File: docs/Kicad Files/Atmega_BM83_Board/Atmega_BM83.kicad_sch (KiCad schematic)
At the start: 34 parts, among them J1 18V, J10 ICE Header, J2 Out to Amp, J3 PWR SW, J4 Volume POT, J5 Pairing BTN, J6 PWR LED, J7 Pair LED, J8 Conn_01x12, J9 Conn_01x12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

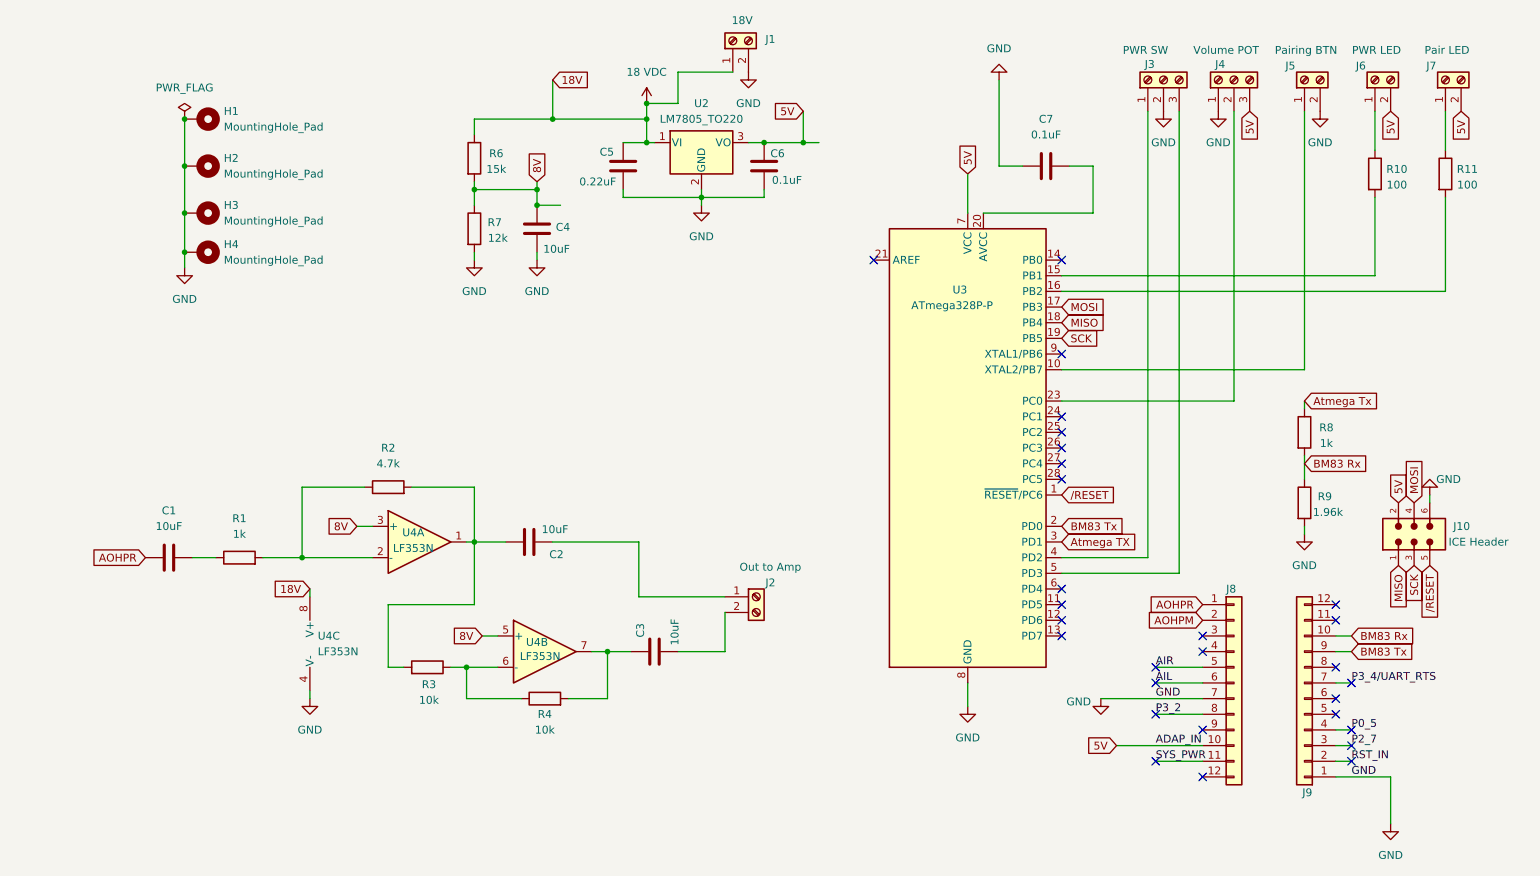
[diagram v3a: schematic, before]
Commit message: initial trace routing for MC/BM83 PCB complete
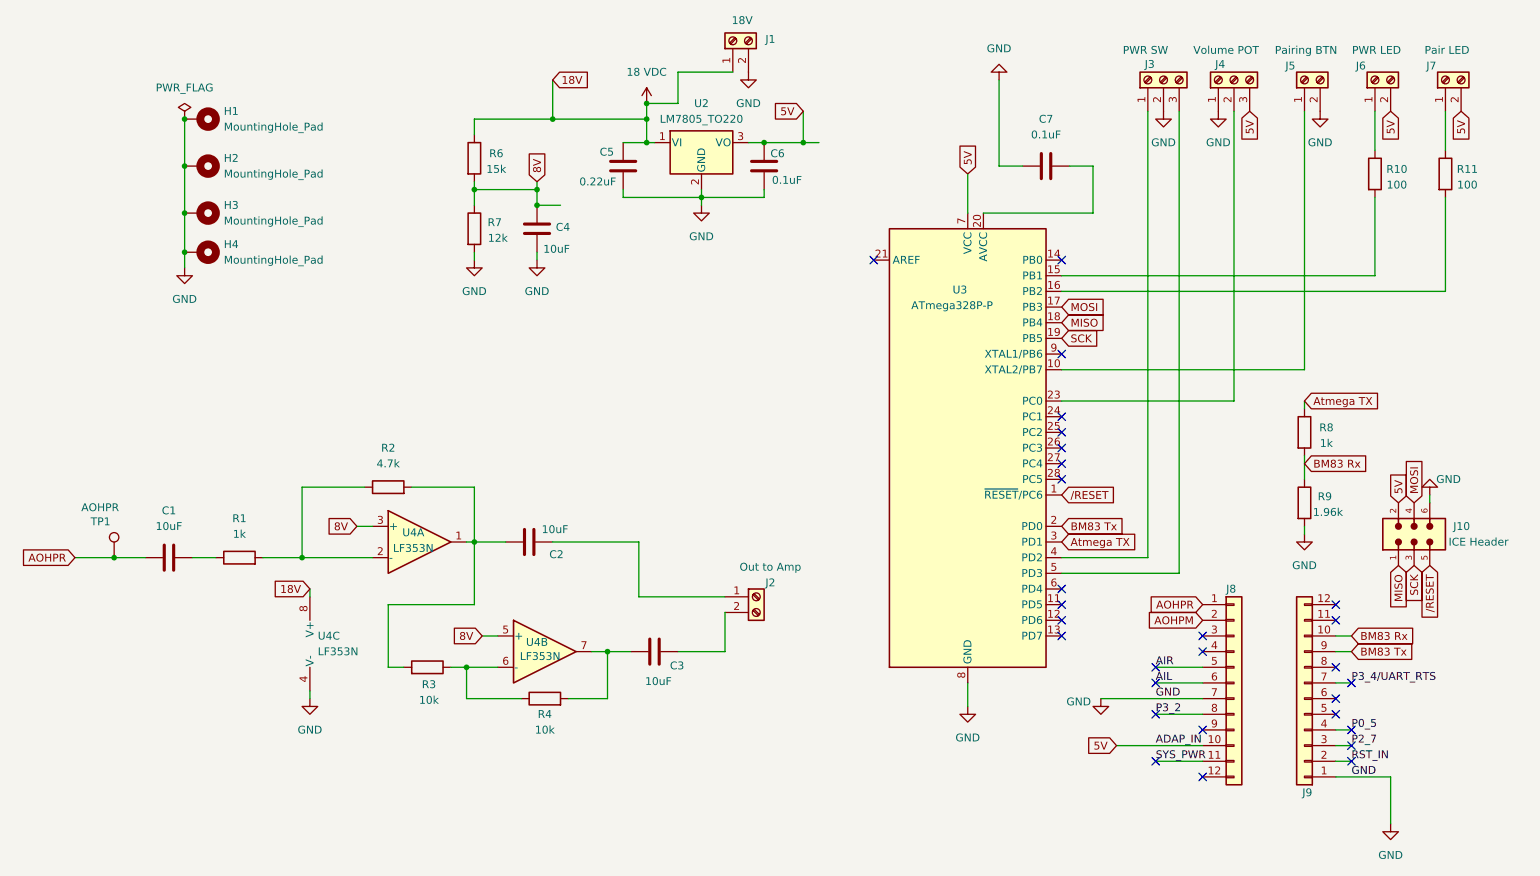
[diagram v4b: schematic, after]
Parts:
- added TP1: AOHPR, TestPoint:TestPoint_THTPad_D2.0mm_Drill1.0mm, symbol Connector:TestPoint
- J10: footprint Custom_Footprints:ICE_Header -> Z_Custom_Footprints:ICE_Header
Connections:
- net Atmega Tx is gone; now on net Atmega TX: R8.1
- net AOHPR: now also TP1.1
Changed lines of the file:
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@@
 	)
 	(junction
+		(at 57.15 102.87)
+		(diameter 0)
+		(color 0 0 0 0)
+	)
+	(junction
 		(at 162.56 35.56)
 		(diameter 0)
@@
 	(wire
 		(pts
+			(xy 57.15 102.87) (xy 62.23 102.87)
+		)
+		(stroke
+			(width 0)
+			(type default)
+		)
+	)
+	(wire
+		(pts
 			(xy 255.27 138.43) (xy 264.16 138.43)
 		)
@@
 	(wire
 		(pts
+			(xy 50.8 102.87) (xy 57.15 102.87)
+		)
+		(stroke
+			(width 0)
+			(type default)
+		)
+	)
+	(wire
+		(pts
 			(xy 101.6 110.49) (xy 115.57 110.49)
 		)
@@
 	(global_label "AOHPR"
 		(shape input)
-		(at 62.23 102.87 180)
+		(at 50.8 102.87 180)
 		(fields_autoplaced yes)
 		(effects
@@
 		)
 		(property "Intersheetrefs" "${INTERSHEET_REFS}"
-			(at 52.9552 102.87 0)
+			(at 41.5252 102.87 0)
 			(effects
 				(font
@@
 		)
 	)
-	(global_label "AOHPR"
+	(global_label "Atmega TX"
 		(shape input)
-		(at 233.68 110.49 180)
+		(at 250.19 77.47 0)
 		(fields_autoplaced yes)
 		(effects
@@
 				(size 1.27 1.27)
 			)
-			(justify right)
+			(justify left)
 		)
 		(property "Intersheetrefs" "${INTERSHEET_REFS}"
-			(at 224.4052 110.49 0)
+			(at 263.2141 77.47 0)
 			(effects
 				(font
 					(size 1.27 1.27)
 				)
-				(justify right)
+				(justify left)
 				(hide yes)
 			)
 		)
 	)
-	(global_label "Atmega Tx"
+	(global_label "AOHPR"
 		(shape input)
-		(at 250.19 77.47 0)
+		(at 233.68 110.49 180)
 		(fields_autoplaced yes)
 		(effects
@@
 				(size 1.27 1.27)
 			)
-			(justify left)
+			(justify right)
 		)
 		(property "Intersheetrefs" "${INTERSHEET_REFS}"
-			(at 263.0327 77.47 0)
+			(at 224.4052 110.49 0)
 			(effects
 				(font
 					(size 1.27 1.27)
 				)
-				(justify left)
+				(justify right)
 				(hide yes)
 			)
@@
 		(dnp no)
 		(property "Reference" "C3"
-			(at 142.494 115.824 0)
+			(at 149.606 120.396 90)
 			(effects
 				(font
@@
 		)
 		(property "Value" "10uF"
-			(at 148.082 117.094 0)
+			(at 147.574 122.936 90)
 			(effects
 				(font
@@
 			)
 		)
-		(property "Footprint" "Custom_Footprints:ICE_Header"
+		(property "Footprint" "Z_Custom_Footprints:ICE_Header"
 			(at 267.97 99.06 0)
 			(effects
@@
 					(unit 1)
 				)
+			)
+		)
+	)
+	(symbol
+		(lib_id "Connector:TestPoint")
+		(at 57.15 102.87 0)
+		(unit 1)
+		(exclude_from_sim no)
+		(in_bom yes)
+		(on_board yes)
+		(dnp no)
+		(property "Reference" "TP1"
+			(at 53.34 97.028 0)
+			(effects
+				(font
+					(size 1.27 1.27)
+				)
+				(justify left)
+			)
+		)
+		(property "Value" "AOHPR"
+			(at 51.816 94.742 0)
+			(effects
+				(font
+					(size 1.27 1.27)
+				)
+				(justify left)
+			)
+		)
+		(property "Footprint" "TestPoint:TestPoint_THTPad_D2.0mm_Drill1.0mm"
+			(at 62.23 102.87 0)
+			(effects
+				(font
+					(size 1.27 1.27)
+				)
+				(hide yes)
+			)
+		)
+		(property "Datasheet" "~"
+			(at 62.23 102.87 0)
+			(effects
+				(font
+					(size 1.27 1.27)
+				)
+				(hide yes)
+			)
+		)
+		(property "Description" "test point"
+			(at 57.15 102.87 0)
+			(effects
+				(font
+					(size 1.27 1.27)
+				)
+				(hide yes)
+			)
+		)
+		(pin "1"
+		)
+		(instances
+			(project ""
+				(path "/b3cfe92d-97c3-48fc-9671-6e68a58d7c48"
+					(reference "TP1")
+					(unit 1)
+				)

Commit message: final changes to both PCBs before review
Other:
- title: BM83/MC Module -> BT/MC Module
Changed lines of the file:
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@@
 	(paper "A4")
 	(title_block
-		(title "BM83/MC Module")
+		(title "BT/MC Module")
+		(date "2024-10-13")
+		(rev "A")
 	)
 	(junction

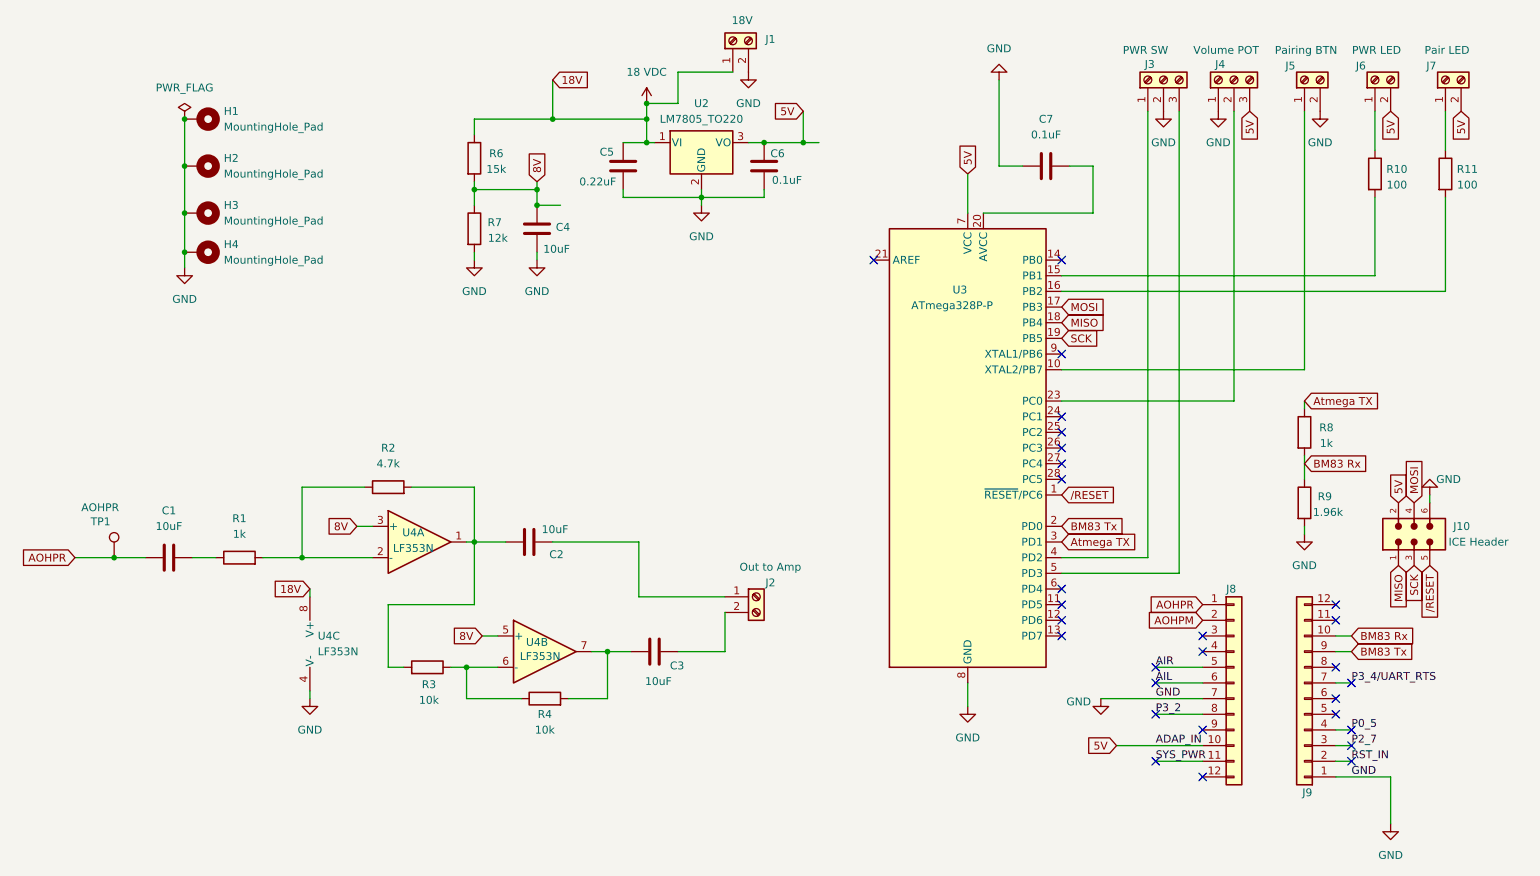
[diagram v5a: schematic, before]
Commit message: widened traces per Mark's suggestion. connected  AVCC and C7 as per datasheet.
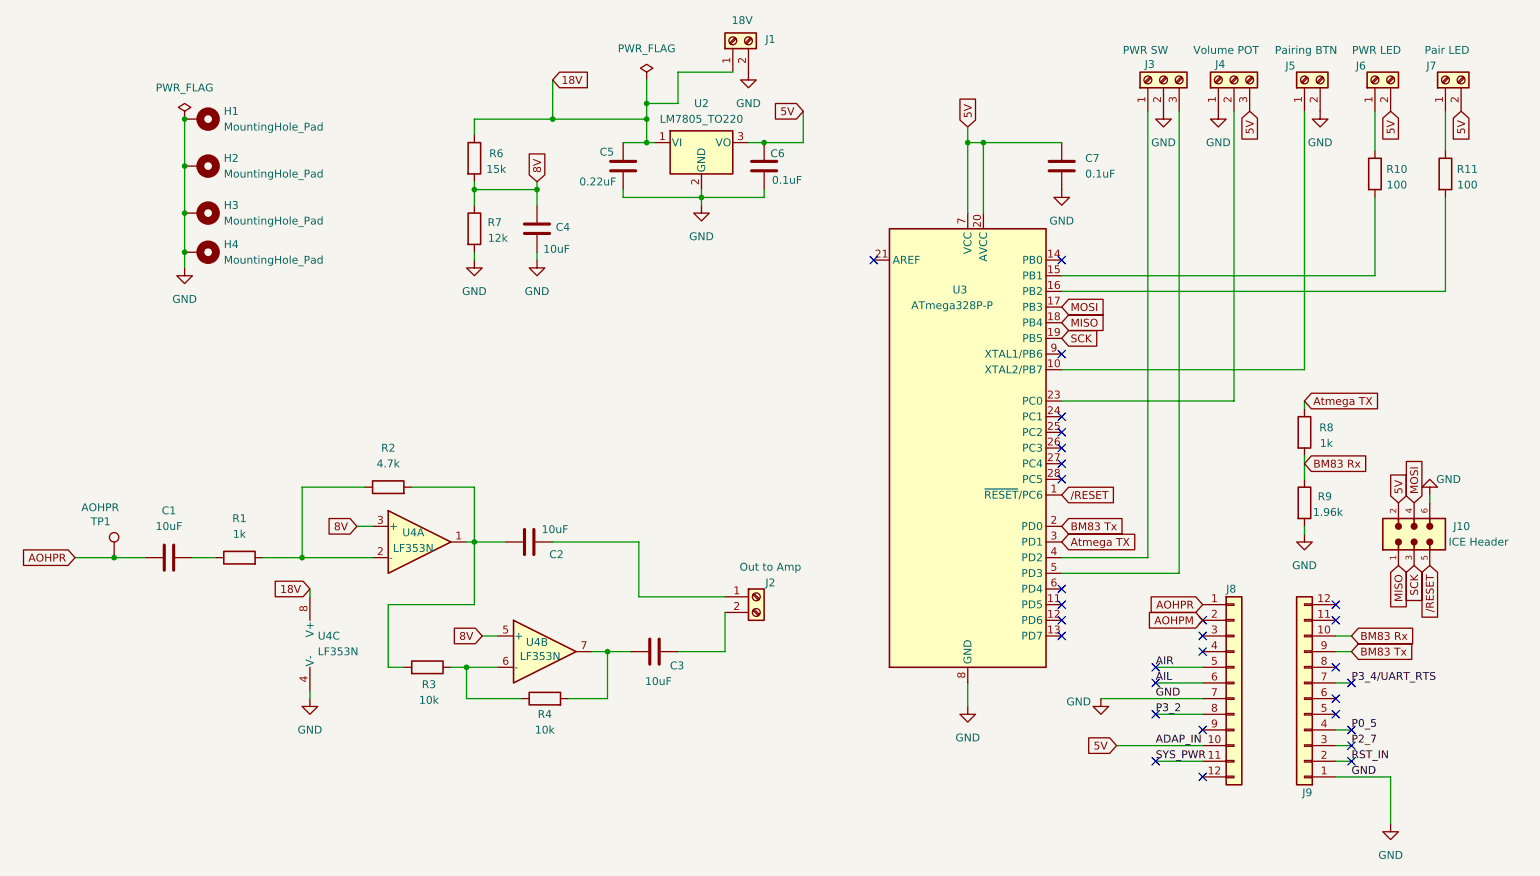
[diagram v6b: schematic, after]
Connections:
- net 5V: now also C7.1, U3.20 (AVCC)
- net GND: now also C7.2; no longer C7.1
- net 18 VDC renamed 18V
- no-connect marks 29 -> 30
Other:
- moved on the sheet: C7

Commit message: updated BT/MC board to reflect changes: removed C2 and C3, changed some cap locations
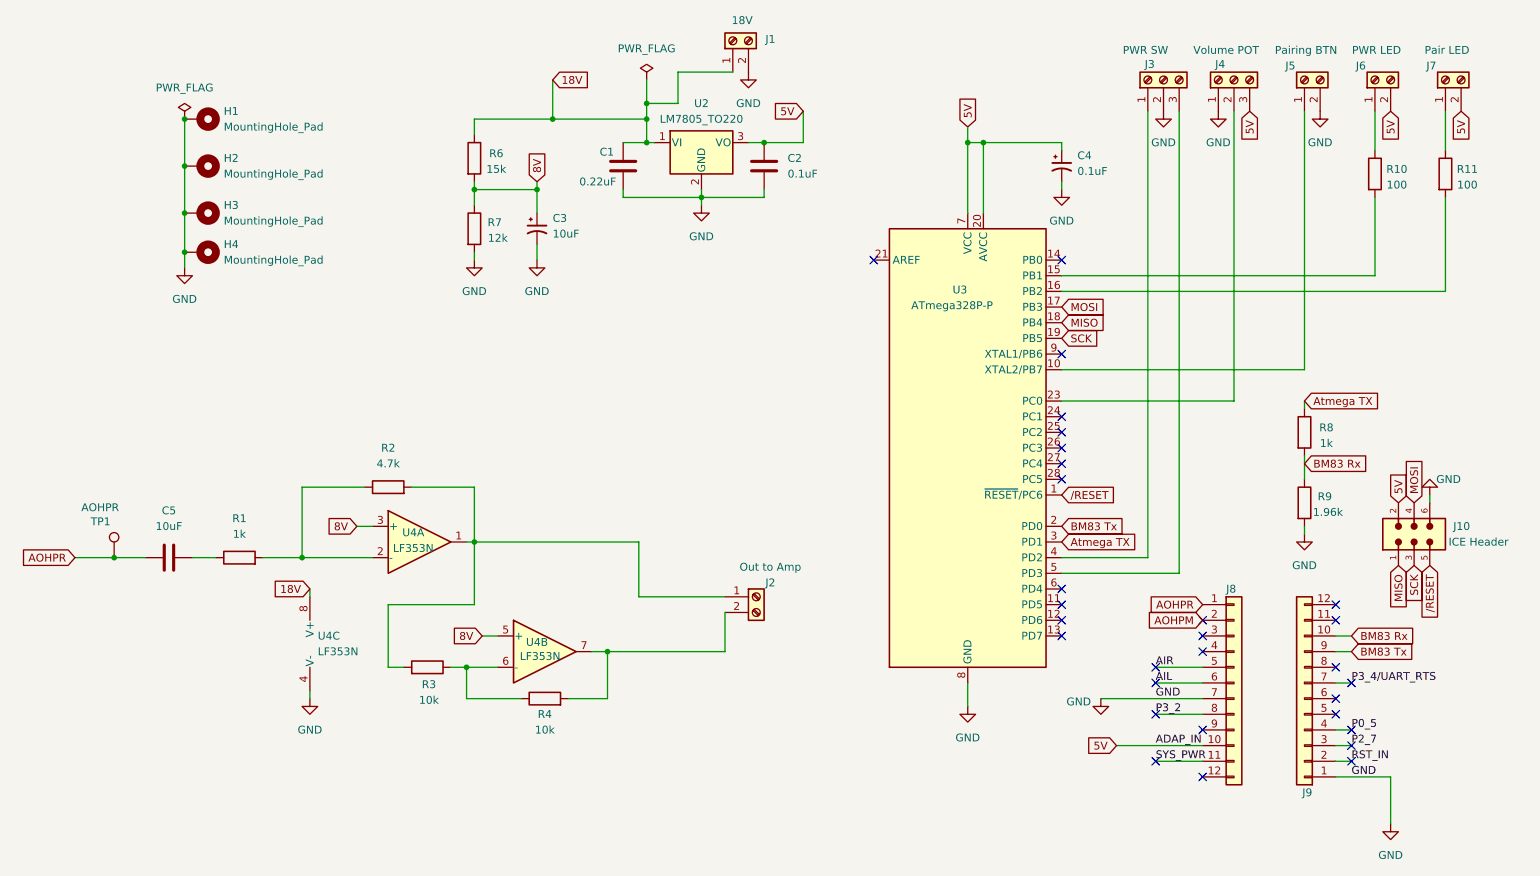
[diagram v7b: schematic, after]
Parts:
- removed C3, C4: 10uF, Capacitor_THT:CP_Radial_Tantal_D5.0mm_P5.00mm, symbol Device:C
- removed C6, C7: 0.1uF, Capacitor_THT:C_Rect_L7.0mm_W2.5mm_P5.00mm, symbol Device:C
- added C3: 10uF, Capacitor_THT:CP_Radial_Tantal_D5.0mm_P5.00mm, symbol Device:C_Polarized_Small_US
- added C4: 0.1uF, Capacitor_THT:C_Rect_L7.0mm_W2.5mm_P5.00mm, symbol Device:C_Polarized_Small_US
- C2: value 10uF -> 0.1uF; footprint Capacitor_THT:CP_Radial_Tantal_D5.0mm_P5.00mm -> Capacitor_THT:C_Rect_L7.0mm_W2.5mm_P5.00mm
- C5: renamed from C1; footprint Capacitor_THT:CP_Radial_Tantal_D5.0mm_P5.00mm -> Capacitor_THT:C_Disc_D6.0mm_W4.4mm_P5.00mm
- renumbered C5 to C1
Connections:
- net 5V: now also C2.1, C4.1
- net 8V: now also C3.1
- net GND: now also C2.2, C3.2, C4.2
- net at J2.1 (Pin_1): now also R2.2, R3.2, U4.1; no longer C2.1
- net at J2.2 (Pin_2): now also R4.2, U4.7
